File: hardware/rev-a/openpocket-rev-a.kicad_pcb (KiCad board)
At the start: 8 copper layers, 115 x 72 mm, 315 parts, among them J1 ER-TFT050A3-2 FFC, J11 5.8 GHz antenna U.FL, J12 push-push microSD, J13 speaker solder pads, J14 SSD1306 128x64 OLED pads, J15 expander developer pads, J18 rotary encoder control pads, J19 ARM switch pads, J2 USB-C, J20 AUX2 three-position switch pa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, J21 AUX3 three-position switch pa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, J22 AUX4 three-position switch pa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, J23 AIL trim pads, J24 ELE trim pads, J25 THR trim pads, J26 RUD trim pads, J3 battery/NTC, J4 speaker connector, J5 master switch, J6 ELRS, J7 left gimbal, J8 right gimbal, J9 menu/UI control pads, Q1 dual protection FET, Q2 Q_BUZZ buzzer MOSFET, U1 ESP32-S3-MINI-1U-N8, U10 display 3V3 buck, U11 analog OSD, U12 OSD 3V3-to-5V, U13 OSD 5V-to-3V3, U14 CVBS TFT controller, U15 AMT boot flash, U16 AMT flash mux, U17 backlight boost, U18 GPIO expander 0x20, U19 GPIO expander 0x21, U2 1S charger/power path, U20 master load switch, U21 I2S speaker amplifier, U22 3V3_SD load switch, U3 1S protector, U4 fuel gauge, U5 3V3 buck-boost, U6 5V boost, U7 5V_VIDEO load switch, U8 5V_DISPLAY load switch, U9 5V_ELRS load switch, Y1 27.000MHz, Y2 27.000MHz

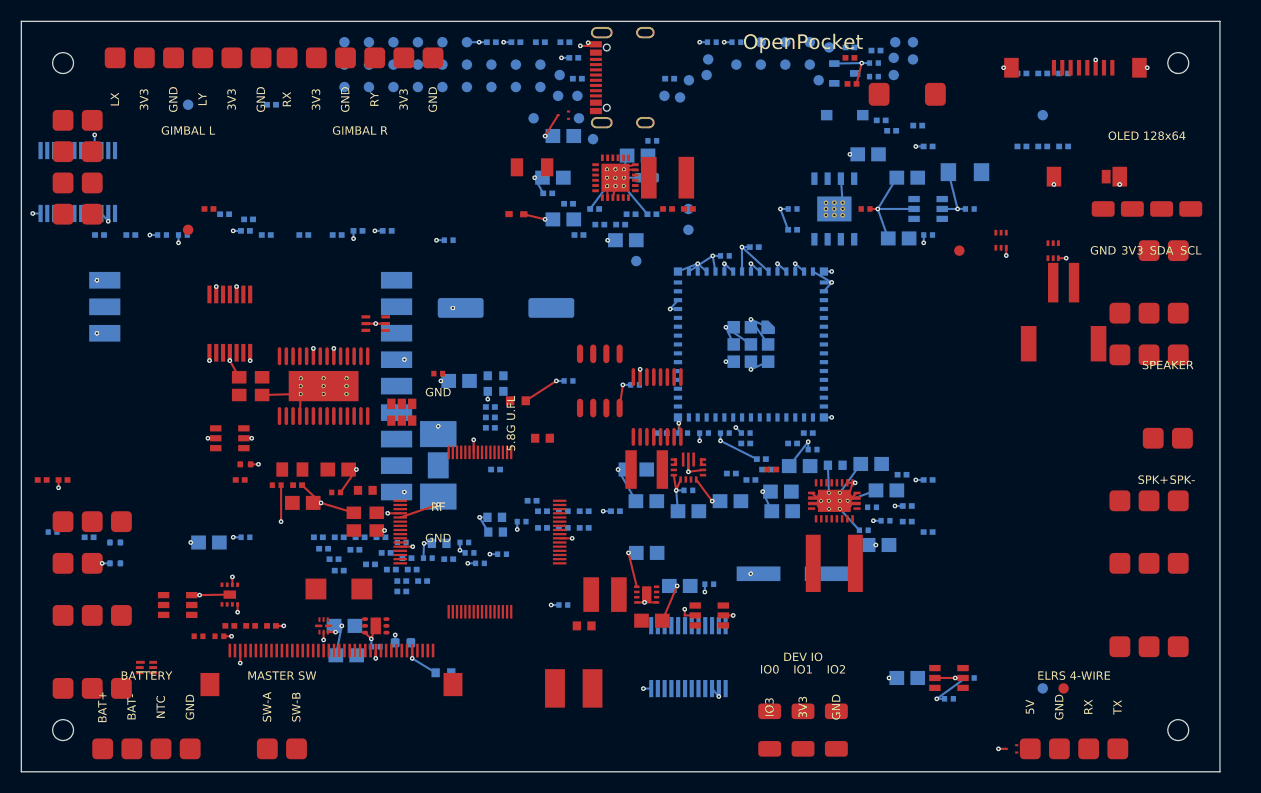
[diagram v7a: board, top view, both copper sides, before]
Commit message: fix(rev-a): retain routing-superior baseline placement
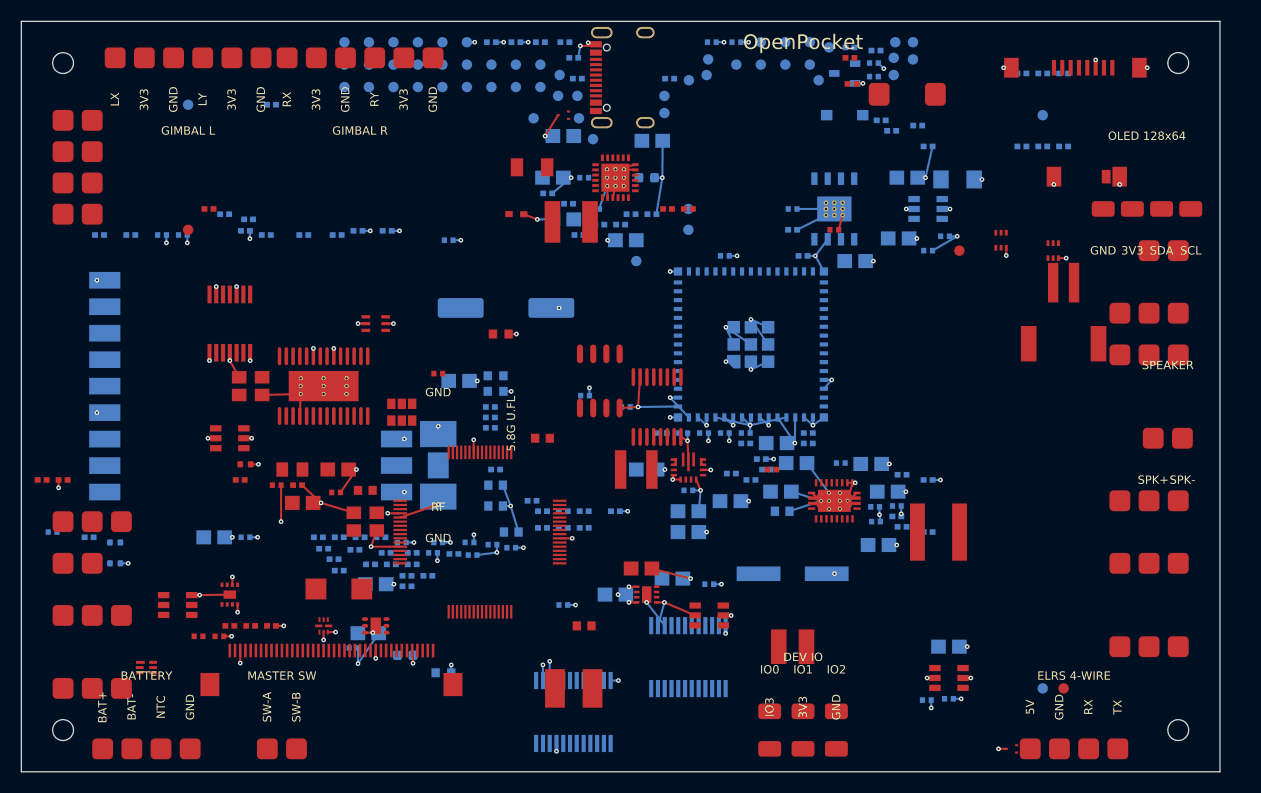
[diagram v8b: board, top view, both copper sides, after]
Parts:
- moved U18 69.6 mm to (53.0, 66.3), turned to 0 degrees
- moved L5 18.7 mm to (74.0, 60.0)
- moved C50 13.8 mm to (72.5, 40.5), turned to 0 degrees
- moved C45 10.7 mm to (82.2, 50.2), turned to 0 degrees
- moved L3 10.4 mm to (88.0, 49.0)
- moved C21 10.3 mm to (80.0, 23.0), turned to 0 degrees
- moved L1 10.2 mm to (52.8, 19.2)
- moved C42 8.14 mm to (81.9, 46.6), turned to 0 degrees
- moved C30 7.43 mm to (54.0, 15.0), turned to 0 degrees
- moved C56 7.39 mm to (34.0, 54.0), turned to 0 degrees
- moved C40 6.73 mm to (73.0, 47.0), turned to 0 degrees
- moved R103 6.61 mm to (46.0, 30.0)
- moved C10 6.49 mm to (45.5, 46.5), turned to 0 degrees
- moved C69 6.22 mm to (40.0, 50.0), turned to 0 degrees
- moved C41 5.20 mm to (78.6, 42.4), turned to 0 degrees
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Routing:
- net GND: track 283.2 -> 272.4 mm, vias 133 -> 145
